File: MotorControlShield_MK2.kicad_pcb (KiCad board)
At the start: 4 copper layers, 93.1 x 97 mm, 66 parts, among them J1 Screw_Terminal_01x02, J2 Screw_Terminal_01x02, J3 Screw_Terminal_01x02, J5 Screw_Terminal_01x02, Q1 IRLIZ44N, Q10 QM6006D, Q2 QM6006D, Q4 QM6006D, Q5 IRLIZ44N, Q6 IRLIZ44N, Q8 IRLIZ44N, Q9 QM6006D, U1 IR2110, U2 LM5109MA, U3 LM78M12_TO252, U5 LM5109MA, U6 IR2110, U7 BTN7960B, U8 BTN7960B

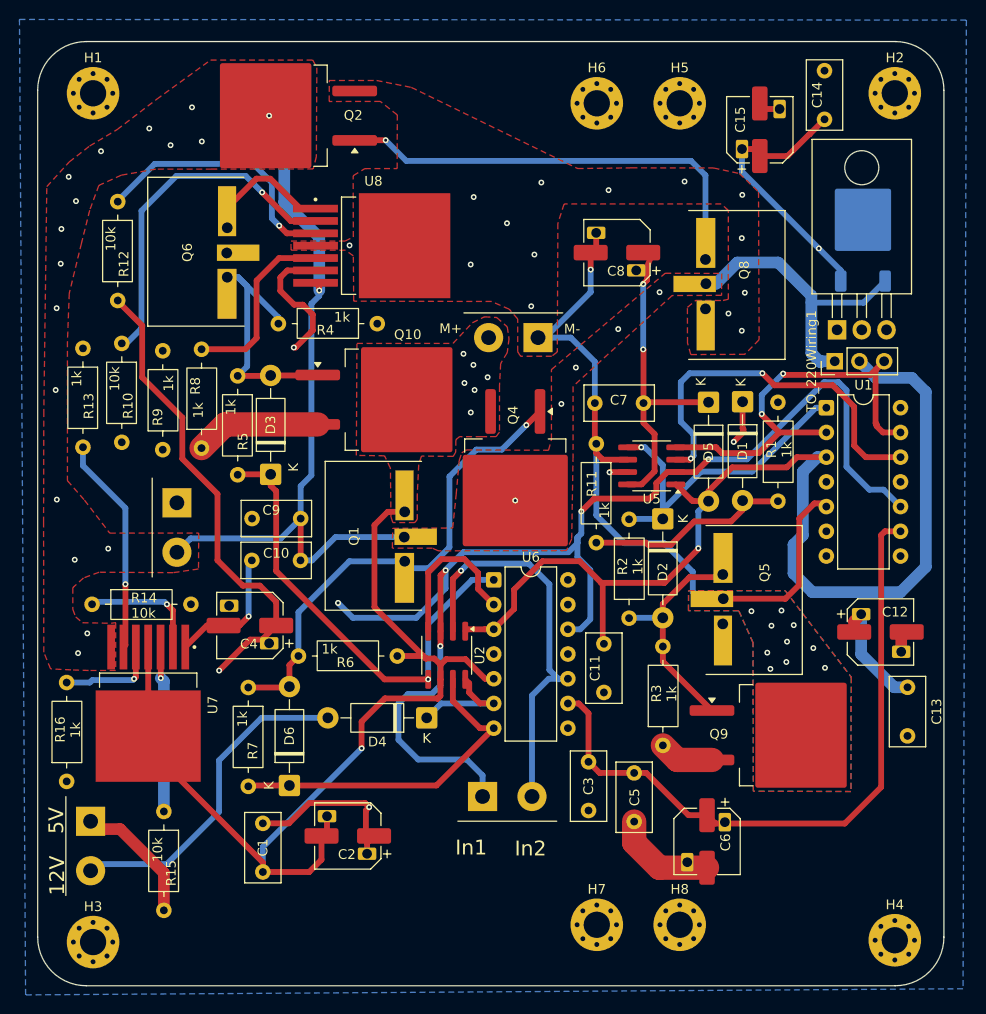
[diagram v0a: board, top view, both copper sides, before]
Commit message: Added pads for extra current
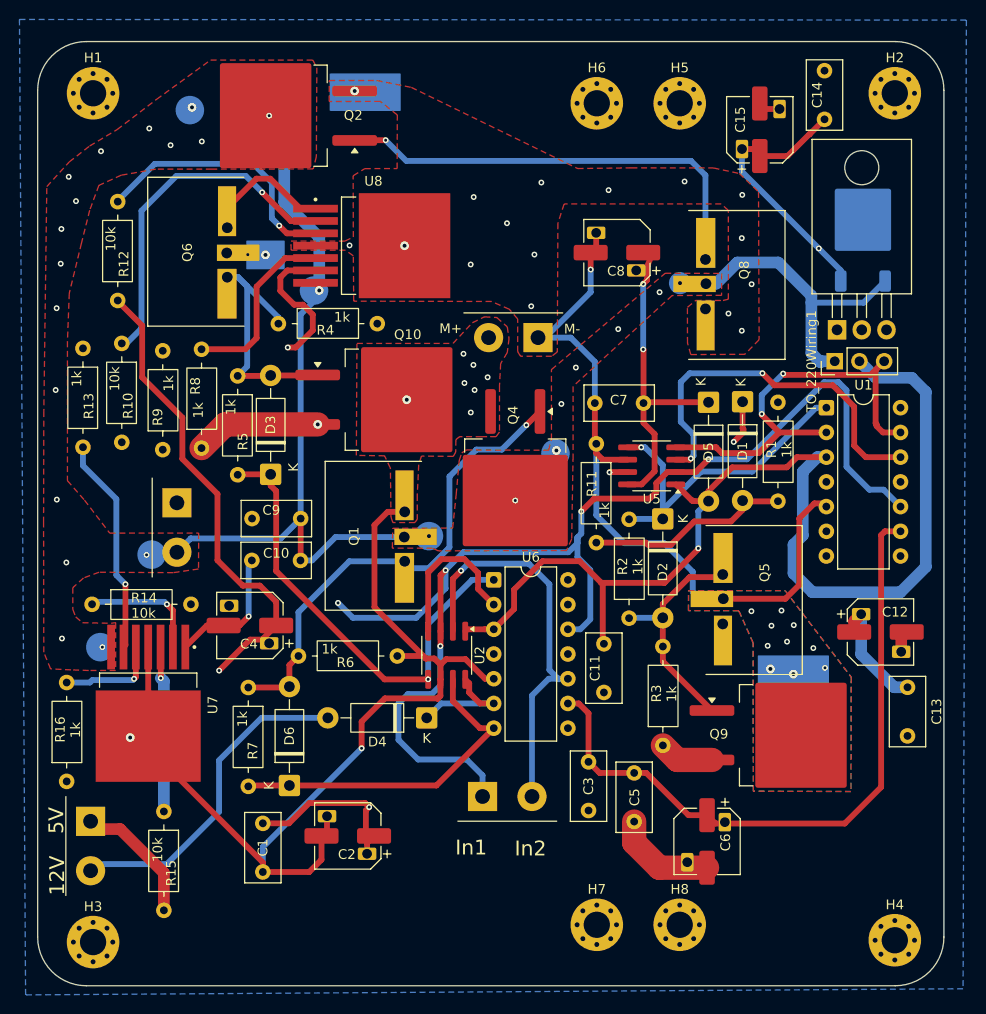
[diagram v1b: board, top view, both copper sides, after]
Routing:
- net Net-(J2-Pin_2): track 125.8 -> 126.7 mm, vias 7 -> 11
- net VDC: vias 23 -> 26
- net Net-(J2-Pin_1): vias 25 -> 27
- net GND: vias 3 -> 4
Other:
- board text added: "Solder thick copper wires on this side to increase current carrying capacity. There are 3 distinct sets of pads, one for each high current net."

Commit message: Made self contained footprints
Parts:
- AMS11173V3: footprint Package_TO_SOT_THT:TO-220-3_Horizontal_TabDown -> Footprints:TO-220-3_Horizontal_TabDown
- C1, C10, C11, C13, C14, C3, C5, C7, C9: footprint Capacitor_THT:C_Rect_L7.0mm_W3.5mm_P5.00mm -> Footprints:C_Rect_L7.0mm_W3.5mm_P5.00mm
- C12, C15, C2, C4, C6, C8: footprint termocuplu:CP_Elec_6.3x3.9_COMPOSITE -> Footprints:CP_Elec_6.3x3.9_COMPOSITE
- D1, D2, D3, D4, D5, D6: footprint Diode_THT:D_DO-41_SOD81_P10.16mm_Horizontal -> Footprints:D_DO-41_SOD81_P10.16mm_Horizontal
- H1, H2, H3, H4, H5, H6, H7, H8: footprint MountingHole:MountingHole_2.7mm_M2.5_Pad_Via -> Footprints:MountingHole_2.7mm_M2.5_Pad_Via
- J1, J2, J3, J5: footprint TO220:TerminalBlock_CLEAN_2PIN -> Footprints:TerminalBlock_CLEAN_2PIN
- Q1, Q5, Q6, Q8: footprint TO220:TO-220-3_EXTENDED2 -> Footprints:TO-220-3_EXTENDED2
- Q10, Q2, Q4, Q9: footprint Package_TO_SOT_SMD:TO-263-2 -> Footprints:TO-263-2
- R1, R10, R11, R12, R13, R14, R15, R16, R2, R3, R4, R5, R6, R7, R8, R9: footprint TO220:R_Axial_Clean -> Footprints:R_Axial_Clean
- TO_220Wiring1: footprint Connector_PinHeader_2.54mm:PinHeader_1x03_P2.54mm_Vertical -> Footprints:PinHeader_1x03_P2.54mm_Vertical
- U1, U6: footprint Package_DIP:DIP-14_W7.62mm -> Footprints:DIP-14_W7.62mm
- U2, U5: footprint Package_SO:SOIC-8_3.9x4.9mm_P1.27mm -> Footprints:SOIC-8_3.9x4.9mm_P1.27mm
- U3: footprint Package_TO_SOT_SMD:TO-252-2 -> Footprints:TO-252-2
- U7, U8: footprint termocuplu:IC_BTN7960B -> Footprints:IC_BTN7960B
